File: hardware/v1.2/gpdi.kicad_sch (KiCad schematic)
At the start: 8 parts, among them U1 ECP5-CABGA256, U10 W9825G6KH

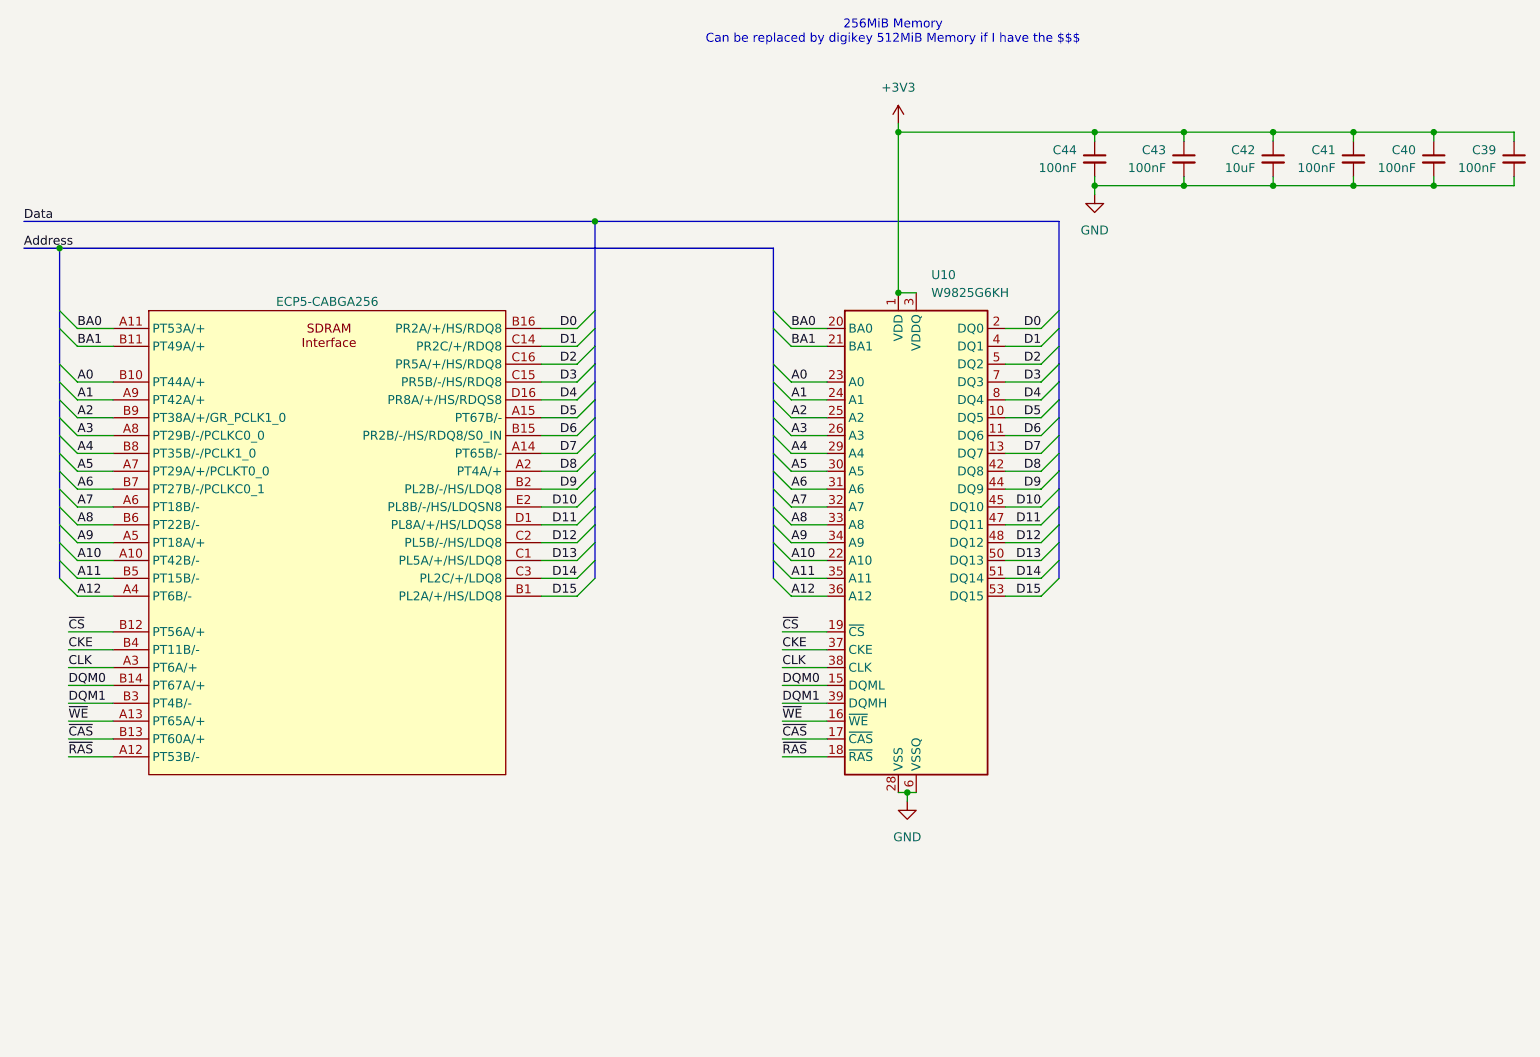
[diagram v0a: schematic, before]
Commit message: Custom ECP5-CABGA256 symbol
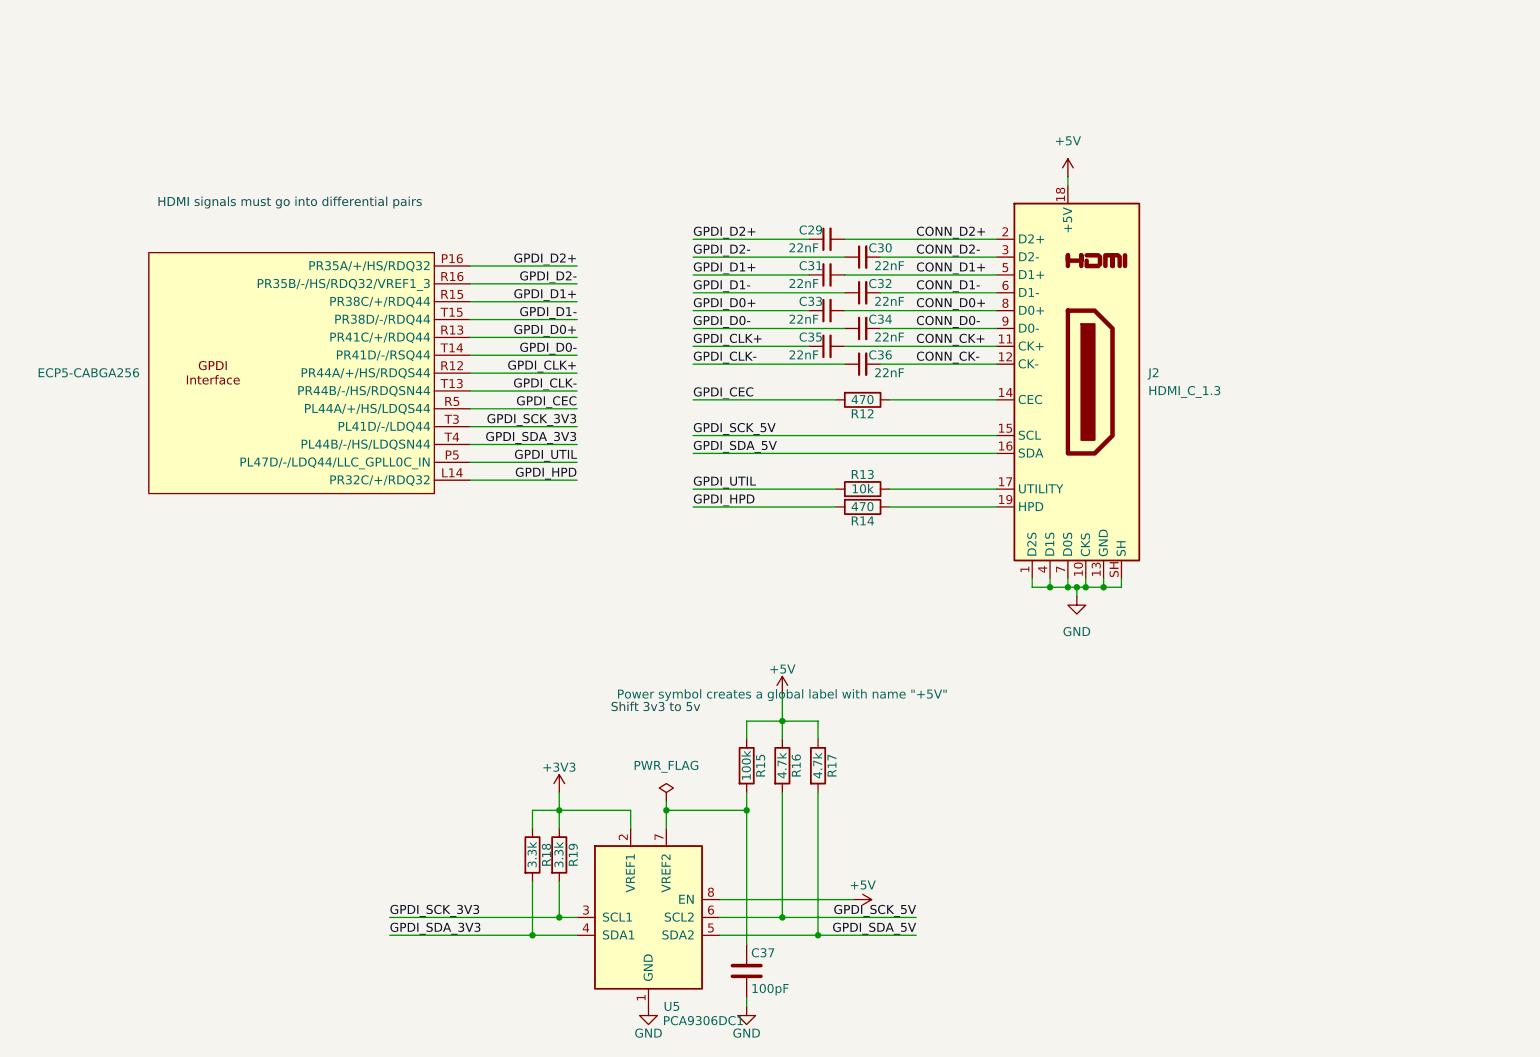
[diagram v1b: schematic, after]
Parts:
- removed C39, C40, C41, C43, C44: 100nF, Capacitor_SMD:C_0402_1005Metric, symbol Device:C_Small
- removed C42: 10uF, Capacitor_SMD:C_0603_1608Metric, symbol Device:C_Small
- removed U1: ECP5-CABGA256, Package_BGA:BGA-256_14.0x14.0mm_Layout16x16_P0.8mm_Ball0.45mm_Pad0.32mm_NSMD, symbol icepi-lib:LFE5U-25F-6BG256x
- removed U10: W9825G6KH, Package_SO:TSOP-II-54_22.2x10.16mm_P0.8mm, symbol Memory_RAM:MT48LC16M16A2P
- added C29, C30, C31, C32, C33, C34, C35, C36: 22nF, Capacitor_SMD:C_0402_1005Metric, symbol Device:C_Small
- added C37: 100pF, Capacitor_SMD:C_0402_1005Metric, symbol Device:C
- added J2: HDMI_C_1.3, icepi-lib:XKB Connection A71-05H4-111N1, symbol Connector:HDMI_C_1.3
- added R12, R14: 470, Resistor_SMD:R_0402_1005Metric, symbol Device:R
- added R13: 10k, Resistor_SMD:R_0402_1005Metric, symbol Device:R
- added R15: 100k, Resistor_SMD:R_0402_1005Metric, symbol Device:R
- added R16, R17: 4.7k, Resistor_SMD:R_0402_1005Metric, symbol Device:R
- added R18, R19: 3.3k, Resistor_SMD:R_0402_1005Metric, symbol Device:R
- added U1: ECP5-CABGA256, Package_BGA:BGA-256_14.0x14.0mm_Layout16x16_P0.8mm_Ball0.45mm_Pad0.32mm_NSMD, symbol icepi-lib:LFE5U-25F-6BG256x
- added U5: PCA9306DC1, Package_SO:VSSOP-8_2.3x2mm_P0.5mm, symbol Interface:PCA9306DC1
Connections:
- net +3V3: now also R18.1, R19.1, U5.2 (VREF1)
- net GND: now also C37.2, J2.1 (D2S), J2.10 (CKS), J2.13 (GND), J2.4 (D1S), J2.7 (D0S), J2.SH, U5.1 (GND)
- new net: C37.1, R15.2, U5.7 (VREF2)
- new net: J2.19 (HPD), R14.1
- new net: J2.14 (CEC), R12.1
- new net: J2.17 (UTILITY), R13.1
- new net +5V: J2.18 (+5V), R15.1, R16.1, R17.1, U5.8 (EN)
- new net CONN_CK+: C35.2, J2.11 (CK+)
- new net CONN_CK-: C36.2, J2.12 (CK-)
- new net CONN_D0+: C33.2, J2.8 (D0+)
- new net CONN_D0-: C34.2, J2.9 (D0-)
- new net CONN_D1+: C31.2, J2.5 (D1+)
- new net CONN_D1-: C32.2, J2.6 (D1-)
- new net CONN_D2+: C29.2, J2.2 (D2+)
- new net CONN_D2-: C30.2, J2.3 (D2-)
- new net GPDI_CEC: R12.2, U1.R5 (PL44A/+/HS/LDQS44)
- new net GPDI_CLK+: C35.1, U1.R12 (PR44A/+/HS/RDQS44)
- new net GPDI_CLK-: C36.1, U1.T13 (PR44B/-/HS/RDQSN44)
- new net GPDI_D0+: C33.1, U1.R13 (PR41C/+/RDQ44)
- new net GPDI_D0-: C34.1, U1.T14 (PR41D/-/RSQ44)
- new net GPDI_D1+: C31.1, U1.R15 (PR38C/+/RDQ44)
- new net GPDI_D1-: C32.1, U1.T15 (PR38D/-/RDQ44)
- new net GPDI_D2+: C29.1, U1.P16 (PR35A/+/HS/RDQ32)
- new net GPDI_D2-: C30.1, U1.R16 (PR35B/-/HS/RDQ32/VREF1_3)
- new net GPDI_HPD: R14.2, U1.L14 (PR32C/+/RDQ32)
- new net GPDI_SCK_3V3: R19.2, U1.T3 (PL41D/-/LDQ44), U5.3 (SCL1)
- new net GPDI_SCK_5V: J2.15 (SCL), R16.2, U5.6 (SCL2)
- new net GPDI_SDA_3V3: R18.2, U1.T4 (PL44B/-/HS/LDQSN44), U5.4 (SDA1)
- new net GPDI_SDA_5V: J2.16 (SDA), R17.2, U5.5 (SDA2)
- new net GPDI_UTIL: R13.2, U1.P5 (PL47D/-/LDQ44/LLC_GPLL0C_IN)
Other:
- note added: "HDMI signals must go into differential pairs"
- note added: "Shift 3v3 to 5v"
- note removed: "256MiB Memory Can be replaced by digikey 512MiB Memory if I have the $$$"
